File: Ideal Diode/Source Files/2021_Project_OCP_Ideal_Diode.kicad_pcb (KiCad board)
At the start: 2 copper layers, 27.9 x 34.1 mm, 21 parts, among them P101 SMD_1POS_8MM, P102 SMD_1POS_8MM, P103 SMD_1POS_8MM, P104 SMD_1POS_8MM, P105 MH_1POS_2.5MM, P106 MH_1POS_2.5MM, P107 MH_1POS_2.5MM, P108 MH_1POS_2.5MM, Q101 PSMNR70-40SSHJ, U101 ZXTR2112F-7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

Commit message: Add files via upload
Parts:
- R101: value RC0603FR-07100RL -> RC0603FR-0716RL
- R104: value ERA-3AEB103V -> RC0603FR-07470RL
- R105: value RMCF0603ZT0R00 -> RC0603FR-07470RL

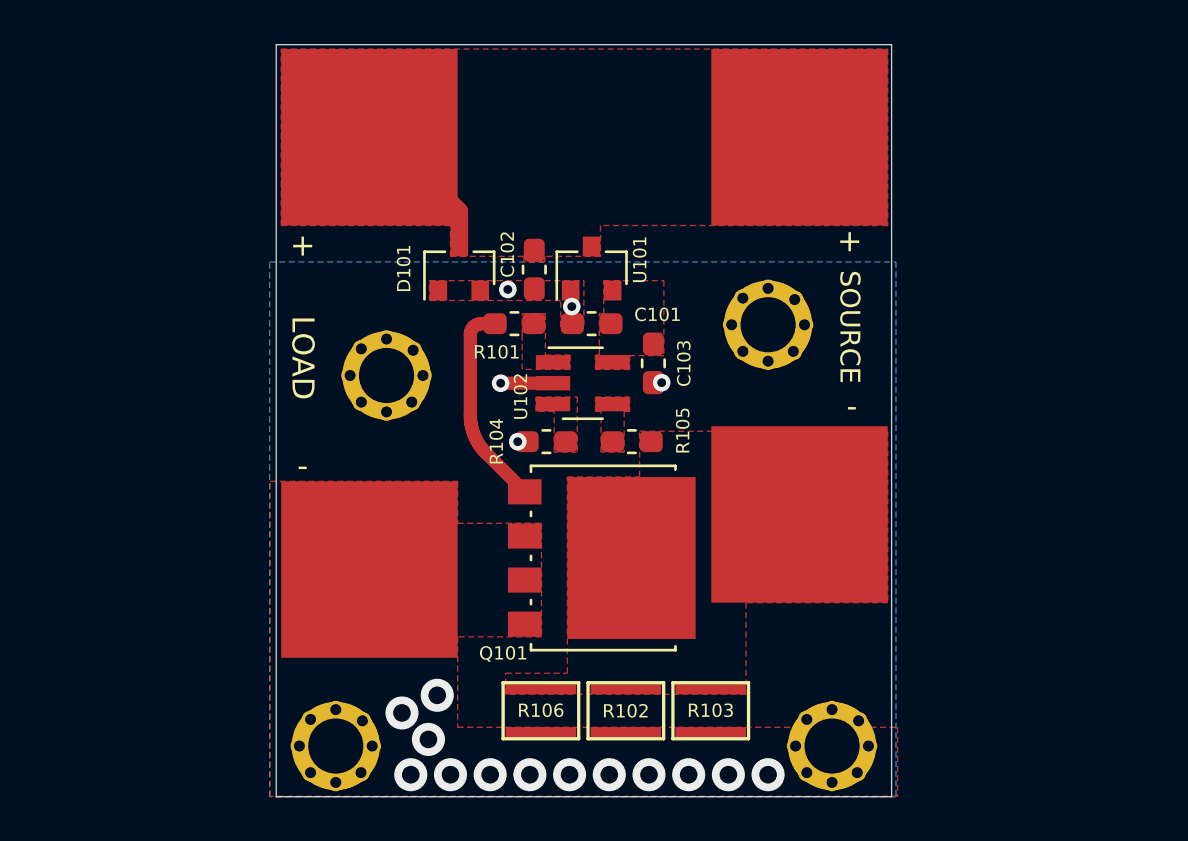
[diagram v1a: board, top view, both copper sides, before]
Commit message: Version A4
Updated to Version A4 of ideal diode
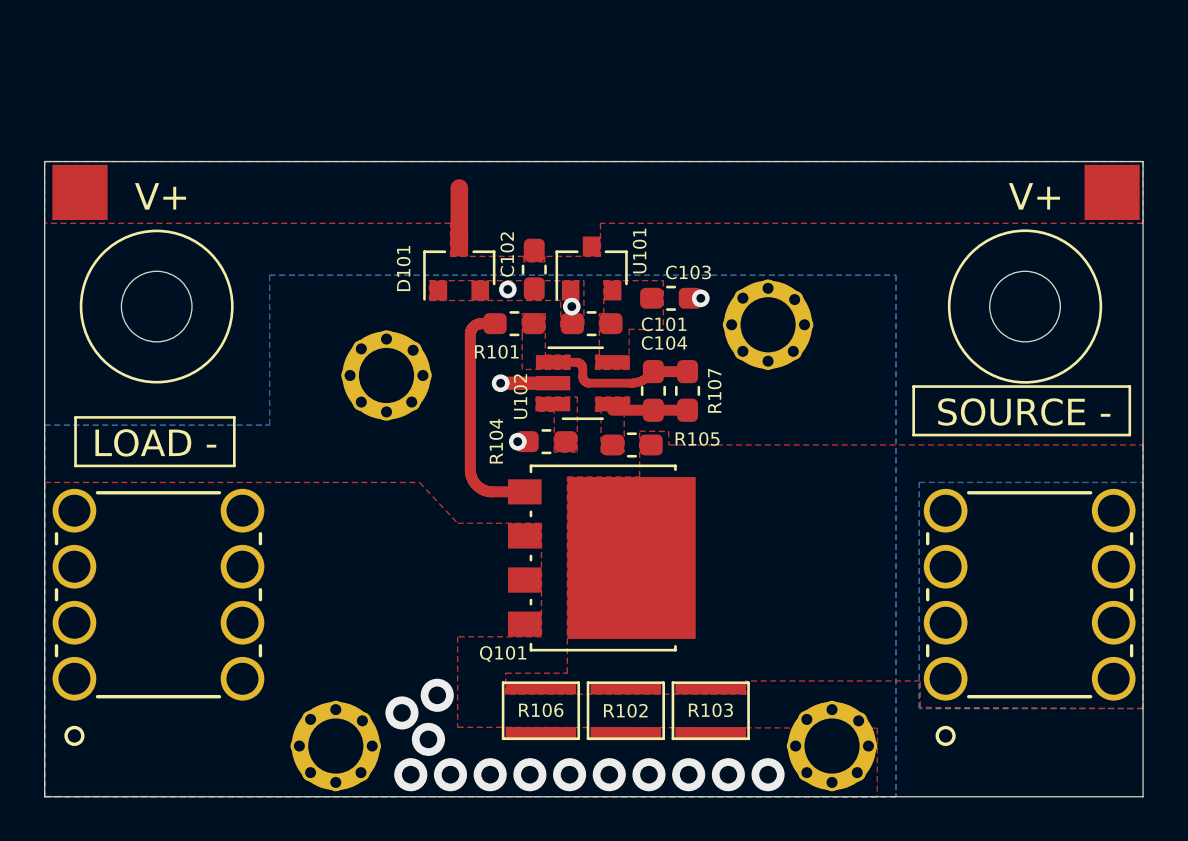
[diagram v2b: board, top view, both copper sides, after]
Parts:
- added C104: C0603C331J5GACTU, Passives:C_0603_Handsolder, F.Cu at (159.6, 118.9)
- added R107: RMCF0603FT300K, Passives:R_0603_Handsolder, F.Cu at (161.2, 118.9)
- added REF**: MountingHole_3.2mm_M3, MountingHole:MountingHole_3.2mm_M3, F.Cu at (176.4, 115.1)
- added REF**: MountingHole_3.2mm_M3, MountingHole:MountingHole_3.2mm_M3, F.Cu at (137.1, 115.1)
- P101, P103: value SMD_1POS_8MM -> 2.5x2.5mm_pad; footprint Connectors_sg:SMD_1POS_8MM -> Terminal Blocks:pad_2.5x2.5mm
- P102, P104: value SMD_1POS_8MM -> 7460305; footprint Connectors_sg:SMD_1POS_8MM -> Terminal Blocks:7460305_HASL
- moved P103 14.4 mm to (180.4, 109.9)
- moved P104 14.3 mm to (133.3, 131.9), turned to 90 degrees
- moved P101 13.4 mm to (133.6, 109.9)
- moved P102 9.97 mm to (172.8, 131.9), turned to 90 degrees
- moved C103 3.06 mm to (160.4, 114.7), turned to 0 degrees
- moved R105 0.15 mm to (158.6, 121.3)
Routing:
- net Net-(C104-Pad2): track 0.00 -> 6.96 mm
- net Net-(C104-Pad1): track 0.00 -> 3.40 mm
- net VBUS: track 4.49 -> 2.42 mm
- net Net-(Q101-Pad1): track 9.45 -> 10.6 mm
- added copper zone on B.Cu, net /CATHODE
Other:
- board size 27.9 x 34.1 mm -> 49.8 x 28.8 mm
- board text added: "20210403_Projects_IdealDiode_A4_00005"
- board text added: "LOAD -"
- board text added: "SOURCE -"
- board text added: "V+"
- board text removed: "+"
- board text removed: "-"
- board text removed: "20210204_Projects_IdealDiode_A2_00003"
- board text removed: "LOAD"
- board text removed: "SOURCE"
